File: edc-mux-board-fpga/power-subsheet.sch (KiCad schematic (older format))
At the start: 3 parts

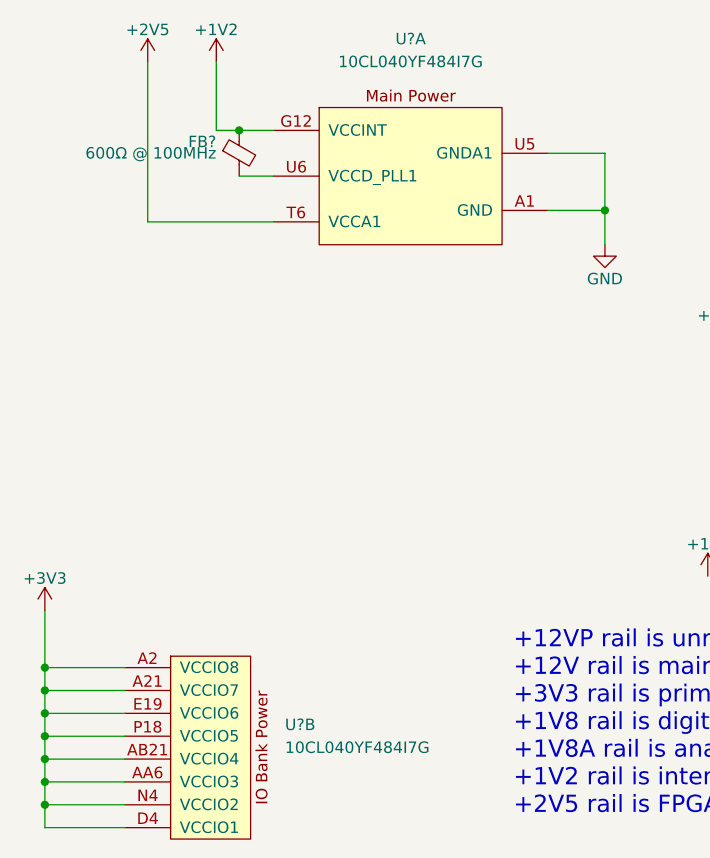
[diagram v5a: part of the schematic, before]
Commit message: Finished FPGA and MCU interconnections.
Finished up interrupt wiring
Fixed a few missing connections
Annotated Schematic
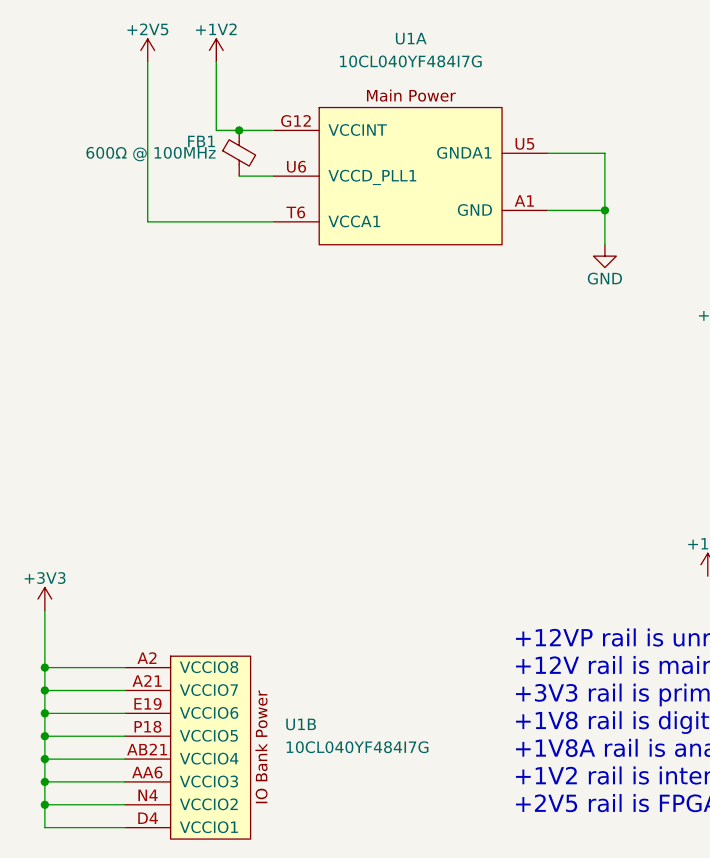
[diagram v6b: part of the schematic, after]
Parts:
- gave numbers to parts that had none: 2
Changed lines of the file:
@@
 $EndDescr
 $Comp
-L SW-Intel:10CL040YF484I7G U?
+L SW-Intel:10CL040YF484I7G U1
 U 1 1 5CB1DD91
 P 6050 2250
-F 0 "U?" H 6050 2850 50  0000 C CNN
+F 0 "U1" H 6050 2850 50  0000 C CNN
 F 1 "10CL040YF484I7G" H 6050 2750 50  0000 C CNN
 F 2 "SW-Intel:FBGA-484_23.0x23.0mm_Layout22x22_P1.0mm" H 8750 3150 50  0001 C CNN
@@
 $EndComp
 $Comp
-L power:+3V3 #PWR?
+L power:+3V3 #PWR05
 U 1 1 5CC2D266
 P 7700 3050
-F 0 "#PWR?" H 7700 2900 50  0001 C CNN
+F 0 "#PWR05" H 7700 2900 50  0001 C CNN
 F 1 "+3V3" H 7700 3190 50  0000 C CNN
 F 2 "" H 7700 3050 50  0001 C CNN
@@
 $EndComp
 $Comp
-L power:+1V8 #PWR?
+L power:+1V8 #PWR06
 U 1 1 5CC2D9F8
 P 8050 3200
-F 0 "#PWR?" H 8050 3050 50  0001 C CNN
+F 0 "#PWR06" H 8050 3050 50  0001 C CNN
 F 1 "+1V8" H 8050 3340 50  0000 C CNN
 F 2 "" H 8050 3200 50  0001 C CNN
@@
 $EndComp
 $Comp
-L SW-power:+1V8A #+1V8A?
+L SW-power:+1V8A #+1V8A01
 U 1 1 5CC2E124
 P 8550 3200
-F 0 "#+1V8A?" H 9300 2900 60  0001 C CNN
+F 0 "#+1V8A01" H 9300 2900 60  0001 C CNN
 F 1 "+1V8A" H 8550 3350 50  0000 C CNN
 F 2 "" H 8550 3200 60  0001 C CNN
@@
 $EndComp
 $Comp
-L power:GND #PWR?
+L power:GND #PWR07
 U 1 1 5CC2E87F
 P 8100 3800
-F 0 "#PWR?" H 8100 3550 50  0001 C CNN
+F 0 "#PWR07" H 8100 3550 50  0001 C CNN
 F 1 "GND" H 8100 3650 50  0000 C CNN
 F 2 "" H 8100 3800 50  0001 C CNN
@@
 +12VP rail is unregulated power input to board.\n+12V rail is main power supply for board. Produced from +12VP rail.\n+3V3 rail is primary digital supply and IO voltage reference\n+1V8 rail is digital supply\n+1V8A rail is analog supply for CODECs. Connect to +1V8 using ferrite bead\n+1V2 rail is internal core voltage for FGPA\n+2V5 rail is FPGA PLL Analog Supply
 $Comp
-L power:+12V #PWR?
+L power:+12V #PWR04
 U 1 1 5CC7BE37
 P 7400 3000
-F 0 "#PWR?" H 7400 2850 50  0001 C CNN
+F 0 "#PWR04" H 7400 2850 50  0001 C CNN
 F 1 "+12V" H 7400 3140 50  0000 C CNN
 F 2 "" H 7400 3000 50  0001 C CNN
@@
 $EndComp
 $Comp
-L SW-Intel:10CL040YF484I7G U?
+L SW-Intel:10CL040YF484I7G U1
 U 2 1 5CB65921
 P 5000 4750
-F 0 "U?" H 5500 4850 50  0000 L CNN
+F 0 "U1" H 5500 4850 50  0000 L CNN
 F 1 "10CL040YF484I7G" H 5500 4750 50  0000 L CNN
 F 2 "SW-Intel:FBGA-484_23.0x23.0mm_Layout22x22_P1.0mm" H 7700 5650 50  0001 C CNN
@@
 $EndComp
 $Comp
-L power:+1V2 #PWR?
+L power:+1V2 #PWR02
 U 1 1 5CB73B8B
 P 5200 1750
-F 0 "#PWR?" H 5200 1600 50  0001 C CNN
+F 0 "#PWR02" H 5200 1600 50  0001 C CNN
 F 1 "+1V2" H 5200 1890 50  0000 C CNN
 F 2 "" H 5200 1750 50  0001 C CNN
@@
 $EndComp
 $Comp
-L power:+2V5 #PWR?
+L power:+2V5 #PWR01
 U 1 1 5CB747E3
 P 4900 1750
-F 0 "#PWR?" H 4900 1600 50  0001 C CNN
+F 0 "#PWR01" H 4900 1600 50  0001 C CNN
 F 1 "+2V5" H 4900 1890 50  0000 C CNN
 F 2 "" H 4900 1750 50  0001 C CNN
@@
 AR Path="/5CC6CC1A/5CC6D47B/5CB7D07D" Ref="FB?"  Part="1"
 AR Path="/5CC3E5DC/5CB7D07D" Ref="FB?"  Part="1"
-AR Path="/5CC3E5B8/5CB7D07D" Ref="FB?"  Part="1"
-F 0 "FB?" H 5200 2200 50  0000 R CNN
+AR Path="/5CC3E5B8/5CB7D07D" Ref="FB1"  Part="1"
+F 0 "FB1" H 5200 2200 50  0000 R CNN
 F 1 "600Ω @ 100MHz" H 5200 2150 50  0000 R CNN
 F 2 "Capacitor_SMD:C_0805_2012Metric" V 5230 2150 50  0001 C CNN
@@
 	5300 2050 5450 2050
 $Comp
-L power:+3V3 #PWR?
+L power:+3V3 #PWR09
 U 1 1 5CB85315
 P 4450 4150
-F 0 "#PWR?" H 4450 4000 50  0001 C CNN
+F 0 "#PWR09" H 4450 4000 50  0001 C CNN
 F 1 "+3V3" H 4450 4290 50  0000 C CNN
 F 2 "" H 4450 4150 50  0001 C CNN
@@
 Connection ~ 4450 5000
 $Comp
-L power:+12P #PWR?
+L power:+12P #PWR08
 U 1 1 62666C46
 P 7350 4000
-F 0 "#PWR?" H 7350 3850 50  0001 C CNN
+F 0 "#PWR08" H 7350 3850 50  0001 C CNN
 F 1 "+12P" H 7350 4140 50  0000 C CNN
 F 2 "" H 7350 4000 50  0001 C CNN
@@
 $EndComp
 $Comp
-L power:GND #PWR?
+L power:GND #PWR03
 U 1 1 6573E3B5
 P 6900 2550
-F 0 "#PWR?" H 6900 2300 50  0001 C CNN
+F 0 "#PWR03" H 6900 2300 50  0001 C CNN
 F 1 "GND" H 6900 2400 50  0000 C CNN
 F 2 "" H 6900 2550 50  0001 C CNN

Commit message: starting work on power supply
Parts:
- added U? (x2): EP5358HUI, SW-Intel:ENPIRION_QFN16_2.5x2.25x1.1mm-0.4mm, symbol SW-Intel:EP5358HUI
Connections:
- new net: U?.2 (PGND), U?.3 (PGND) (x2)
- new net: U?.7 (VOUT), U?.8 (VOUT) (x2)
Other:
- note added: "1V2\nfed from 3V3"
- note added: "2V5\nfed from 3V3"
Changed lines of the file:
@@
 Wire Wire Line
 	6900 2400 6900 2550
+$Comp
+L SW-Intel:EP5358HUI U?
+U 1 1 5CBAD4B4
+P 2950 3000
+F 0 "U?" H 2750 2650 50  0000 C CNN
+F 1 "EP5358HUI" H 2950 3400 50  0000 C CNN
+F 2 "SW-Intel:ENPIRION_QFN16_2.5x2.25x1.1mm-0.4mm" H 2750 2650 50  0001 C CNN
+F 3 "https://www.intel.com/content/dam/www/programmable/us/en/pdfs/literature/ds/ep5358xui_03541.pdf" H 2750 2650 50  0001 C CNN
+F 4 "2.4V-5.5V in, 1.8-3.3V out @ 600mA" H 2950 3000 50  0001 C CNN "Characteristics"
+	1    2950 3000
+	1    0    0    -1
+$EndComp
+$Comp
+L SW-Intel:EP5358HUI U?
+U 1 1 5CBAE385
+P 2950 3900
+F 0 "U?" H 2750 3550 50  0000 C CNN
+F 1 "EP5358HUI" H 2950 4300 50  0000 C CNN
+F 2 "SW-Intel:ENPIRION_QFN16_2.5x2.25x1.1mm-0.4mm" H 2750 3550 50  0001 C CNN
+F 3 "https://www.intel.com/content/dam/www/programmable/us/en/pdfs/literature/ds/ep5358xui_03541.pdf" H 2750 3550 50  0001 C CNN
+F 4 "2.4V-5.5V in, 1.8-3.3V out @ 600mA" H 2950 3900 50  0001 C CNN "Characteristics"
+	1    2950 3900
+	1    0    0    -1
+$EndComp
+Text Notes 3600 2900 0    50   ~ 0
+1V2\nfed from 3V3
+Text Notes 3600 3900 0    50   ~ 0
+2V5\nfed from 3V3
 $EndSCHEMATC

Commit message: Finished off power supplies and decoupling capacitors.
Decoupling calculations for the FPGA are found in 
../fpga-decoupling-calculations
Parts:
- added C1, C2, C3: 4.7uF X7R, Capacitor_SMD:C_0603_1608Metric, symbol Device:C_Small
- added C10, C11, C12, C13, C14, C15, C16, C17, C18, C19, C20, C21, C22, C23, C24, C25, C27, C28, C30, C31, C33, C36, C7, C8, C9: 4.7nF X7R, Capacitor_SMD:C_0402_1005Metric, symbol Device:C_Small
- added C100, C101, C102, C103, C104, C105, C106, C47, C84, C86, C88, C90, C92, C97, C98, C99: 1uF X7R, Capacitor_SMD:C_0603_1608Metric, symbol Device:C_Small
- added C107, C108, C109, C110, C111, C52, C94: 47uF, symbol Device:CP1_Small
- added C26, C29, C32, C35, C38, C40, C43, C46, C49, C51, C54, C56, C58, C59, C61: 10nF X7R, Capacitor_SMD:C_0402_1005Metric, symbol Device:C_Small
- added C34, C37, C39, C42, C45, C48, C50, C53, C55, C57: 47nF X7R, Capacitor_SMD:C_0603_1608Metric, symbol Device:C_Small
- added C4, C5, C6: 10uF X7R, Capacitor_SMD:C_1206_3216Metric, symbol Device:C_Small
- added C41, C44, C60, C62, C63, C64, C65, C66, C67, C68, C69, C70, C71, C72, C73, C74, C75, C76, C77, C78, C79, C81: 100nF X7R, Capacitor_SMD:C_0603_1608Metric, symbol Device:C_Small
- added C80, C82, C83, C85, C87, C89, C91, C93, C95, C96: 220nF X7R, Capacitor_SMD:C_0603_1608Metric, symbol Device:C_Small
- added FB1: 600Ω @ 100MHz, Capacitor_SMD:C_0805_2012Metric, symbol Device:Ferrite_Bead_Small
- added U1: R-78B12-2.0, Converter_DCDC:Converter_DCDC_RECOM_R-78B-2.0_THT, symbol Regulator_Switching:R-78B12-2.0
- added U2: R-78B3.3-2.0, Converter_DCDC:Converter_DCDC_RECOM_R-78B-2.0_THT, symbol Regulator_Switching:R-78B3.3-2.0
- added U4: EP5358HUI, SW-Intel:ENPIRION_QFN16_2.5x2.25x1.1mm-0.4mm, symbol SW-Intel:EP5358HUI
- U5: renamed from U?; value EP5358HUI -> EP5358LUI
- U6: renamed from U1; Description (none) -> Intel Cyclone 10 LP FPGA; Manufacturer (none) -> Intel; Manufacturers Part Number (none) -> 10CL040YF484I7G; Package ID (none) -> 484BGA
- gave numbers to parts that had none: 1
- renumbered FB1 to FB2
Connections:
- wire segments 26 -> 350
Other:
- note added: "1V8\nfed from 3V3"
- note added: "FPGA power rail decoupling\nPlace as close to power input pins \nas possible (on back)\nwith the bulk capacitors \ntowards the outside"
- note added: "regulated 12V"
- moved on the sheet: FB2, U3, U5, U6A, U6B
